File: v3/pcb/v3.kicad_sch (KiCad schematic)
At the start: 421 parts, among them J1 USB_C_Receptacle_USB2.0, J2 Conn_01x21, SW1 SW_Push, SW10 SW_Push, SW11 SW_Push, SW12 SW_Push, SW13 SW_Push, SW14 SW_Push, SW15 SW_Push, SW16 SW_Push, SW17 SW_Push, SW18 SW_Push, SW19 SW_Push, SW2 SW_Push, SW20 SW_Push, SW21 SW_Push, SW22 SW_Push, SW23 SW_Push, SW24 SW_Push, SW25 SW_Push, SW26 SW_Push, SW27 SW_Push, SW28 SW_Push, SW29 SW_Push, SW3 SW_Push, SW30 SW_Push, SW31 SW_Push, SW32 SW_Push, SW33 SW_Push, SW34 SW_Push, SW35 SW_Push, SW36 SW_Push, SW37 SW_Push, SW38 SW_Push, SW39 SW_Push, SW4 SW_Push, SW40 SW_Push, SW41 SW_Push, SW42 SW_Push, SW43 SW_Push, SW44 SW_Push, SW45 SW_Push, SW46 SW_Push, SW47 SW_Push, SW48 SW_Push, SW49 SW_Push, SW5 SW_Push, SW50 SW_Push, SW51 SW_Push, SW52 SW_Push, SW53 SW_Push, SW54 SW_Push, SW55 SW_Push, SW56 SW_Push, SW57 SW_Push, SW58 SW_Push, SW59 SW_Push, SW6 SW_Push, SW60 SW_Push, SW61 SW_Push, SW62 SW_Push, SW63 SW_Push, SW64 SW_Push, SW65 SW_Push, SW66 SW_Push, SW67 SW_Push, SW68 SW_Push, SW69 SW_Push, SW7 SW_Push, SW70 SW_Push, SW71 SW_Push, SW72 SW_Push, SW73 SW_Push, SW74 SW_Push, SW75 SW_Push, SW76 SW_Push, SW77 SW_Push, SW78 SW_Push, SW79 SW_Push, SW8 SW_Push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

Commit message: Add some part numbers and start adding row tracks
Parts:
- C1, C10, C11, C12, C13, C14, C15, C16, C17, C18, C19, C2, C20, C21, C22, C23, C24, C25, C26, C27, C28, C29, C3, C30, C31, C32, C33, C34, C35, C36, C37, C38, C39, C4, C40, C41, C42, C43, C44, C45, C46, C47, C48, C49, C5, C50, C51, C52, C53, C54, C55, C56, C57, C58, C59, C6, C60, C61, C62, C63, C64, C65, C66, C67, C68, C69, C7, C70, C71, C72, C73, C74, C75, C76, C77, C78, C79, C8, C80, C81, C82, C83, C84, C85, C86, C87, C88, C89, C9, C90, C91, C92, C93, C94, C95, C96, C97, C98, C99: LCSC Part C14663 -> C14663
- D1, D10, D11, D12, D13, D14, D15, D16, D17, D18, D19, D2, D20, D21, D22, D23, D24, D25, D26, D27, D28, D29, D3, D30, D31, D32, D33, D34, D35, D36, D37, D38, D39, D4, D40, D41, D42, D43, D44, D45, D46, D47, D48, D49, D5, D50, D51, D52, D53, D54, D55, D56, D57, D58, D59, D6, D60, D61, D62, D63, D64, D65, D66, D67, D68, D69, D7, D70, D71, D72, D73, D74, D75, D76, D77, D78, D79, D8, D80, D81, D82, D83, D84, D85, D86, D87, D88, D89, D9, D90, D91, D92, D93, D94, D95, D96, D97, D98, D99: footprint Diode_SMD:D_SOD-323F -> prettylib:D_SOD-123; symbol Device:D -> Diode:1N4148; LCSC Part (none) -> C81598
- FB1: LCSC C668229 -> (none); LCSC Part (none) -> C668229
- J1: LCSC Part (none) -> C165948
- R1, R2: LCSC C104384 -> (none); LCSC Part (none) -> C104384
- RGB1, RGB10, RGB11, RGB12, RGB13, RGB14, RGB15, RGB16, RGB17, RGB18, RGB19, RGB2, RGB20, RGB21, RGB22, RGB23, RGB24, RGB25, RGB26, RGB27, RGB28, RGB29, RGB3, RGB30, RGB31, RGB32, RGB33, RGB34, RGB35, RGB36, RGB37, RGB38, RGB39, RGB4, RGB40, RGB41, RGB42, RGB43, RGB44, RGB45, RGB46, RGB47, RGB48, RGB49, RGB5, RGB50, RGB51, RGB52, RGB53, RGB54, RGB55, RGB56, RGB57, RGB58, RGB59, RGB6, RGB60, RGB61, RGB62, RGB63, RGB64, RGB65, RGB66, RGB67, RGB68, RGB69, RGB7, RGB70, RGB71, RGB72, RGB73, RGB74, RGB75, RGB76, RGB77, RGB78, RGB79, RGB8, RGB80, RGB81, RGB82, RGB83, RGB84, RGB85, RGB86, RGB87, RGB88, RGB89, RGB9, RGB90, RGB91, RGB92, RGB93, RGB94, RGB95, RGB96, RGB97, RGB98, RGB99: JLCPCB BOM 0 -> 1; LCSC Part (none) -> C5149201
- RGB_LOGO1, RGB_LOGO2, RGB_LOGO3, RGB_LOGO4: LCSC Part (none) -> C5149201
- SW1, SW10, SW11, SW12, SW13, SW14, SW15, SW16, SW17, SW18, SW19, SW2, SW20, SW21, SW22, SW23, SW24, SW25, SW26, SW27, SW28, SW29, SW3, SW30, SW31, SW32, SW33, SW34, SW35, SW36, SW37, SW38, SW39, SW4, SW40, SW41, SW42, SW43, SW44, SW45, SW46, SW47, SW48, SW49, SW5, SW50, SW51, SW52, SW53, SW54, SW55, SW56, SW57, SW58, SW59, SW6, SW60, SW61, SW62, SW63, SW64, SW65, SW66, SW67, SW68, SW69, SW7, SW70, SW71, SW72, SW73, SW74, SW75, SW76, SW77, SW78, SW79, SW8, SW80, SW81, SW82, SW83, SW84, SW85, SW86, SW87, SW88, SW89, SW9, SW90, SW91, SW92, SW93, SW94, SW95, SW96, SW97, SW98, SW99: LCSC Part (none) -> C5184526
- U2: LCSC Part (none) -> C139353

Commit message: PCB might be ready for manufacturing
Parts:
- SW1, SW10, SW11, SW12, SW13, SW14, SW15, SW16, SW17, SW18, SW19, SW2, SW20, SW21, SW22, SW23, SW24, SW25, SW26, SW28, SW29, SW3, SW30, SW31, SW32, SW33, SW34, SW35, SW36, SW37, SW38, SW39, SW4, SW40, SW41, SW42, SW43, SW44, SW45, SW46, SW47, SW48, SW49, SW5, SW50, SW52, SW53, SW54, SW55, SW56, SW57, SW58, SW59, SW6, SW60, SW61, SW62, SW63, SW65, SW66, SW67, SW68, SW69, SW7, SW70, SW71, SW72, SW73, SW74, SW75, SW76, SW77, SW78, SW79, SW8, SW80, SW81, SW82, SW83, SW84, SW85, SW87, SW88, SW89, SW9, SW90, SW93, SW94, SW95, SW96, SW97, SW99: footprint prettylib:MX_KAILH_SOCKET_1U -> zekeyboard:MX_KAILH_SOCKET_1U_NONFLIP
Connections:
- no-connect marks 38 -> 36

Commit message: Ready for production
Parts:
- C1, C10, C11, C12, C13, C14, C15, C16, C17, C18, C19, C2, C20, C21, C22, C23, C24, C25, C26, C27, C28, C29, C3, C30, C31, C32, C33, C34, C35, C36, C37, C38, C39, C4, C40, C41, C42, C43, C44, C45, C46, C47, C48, C49, C5, C50, C51, C52, C53, C54, C55, C56, C57, C58, C59, C6, C60, C61, C62, C63, C64, C65, C66, C67, C68, C69, C7, C70, C71, C72, C73, C74, C75, C76, C77, C78, C79, C8, C80, C81, C82, C83, C84, C85, C86, C87, C88, C89, C9, C90, C91, C92, C93, C94, C95, C96, C97, C98, C99: footprint prettylib:SMD-0603 -> Capacitor_SMD:C_0603_1608Metric; LCSC (none) -> C14663
- D1, D10, D11, D12, D13, D14, D15, D16, D17, D18, D19, D2, D20, D21, D22, D23, D24, D25, D26, D27, D28, D29, D3, D30, D31, D32, D33, D34, D35, D36, D37, D38, D39, D4, D40, D41, D42, D43, D44, D45, D46, D47, D48, D49, D5, D50, D51, D52, D53, D54, D55, D56, D57, D58, D59, D6, D60, D61, D62, D63, D64, D65, D66, D67, D68, D69, D7, D70, D71, D72, D73, D74, D75, D76, D77, D78, D79, D8, D80, D81, D82, D83, D84, D85, D86, D87, D88, D89, D9, D90, D91, D92, D93, D94, D95, D96, D97, D98, D99: footprint prettylib:D_SOD-123 -> Diode_SMD:D_SOD-123; LCSC (none) -> C81598
- FB1: LCSC (none) -> C668229
- J1: LCSC (none) -> C165948
- R1, R2: LCSC (none) -> C104384
- RGB1, RGB10, RGB11, RGB12, RGB13, RGB14, RGB15, RGB16, RGB17, RGB18, RGB19, RGB2, RGB20, RGB21, RGB22, RGB23, RGB24, RGB25, RGB26, RGB27, RGB28, RGB29, RGB3, RGB30, RGB31, RGB32, RGB33, RGB34, RGB35, RGB36, RGB37, RGB38, RGB39, RGB4, RGB40, RGB41, RGB42, RGB43, RGB44, RGB45, RGB46, RGB47, RGB48, RGB49, RGB5, RGB50, RGB51, RGB52, RGB53, RGB54, RGB55, RGB56, RGB57, RGB58, RGB59, RGB6, RGB60, RGB61, RGB62, RGB63, RGB64, RGB65, RGB66, RGB67, RGB68, RGB69, RGB7, RGB70, RGB71, RGB72, RGB73, RGB74, RGB75, RGB76, RGB77, RGB78, RGB79, RGB8, RGB80, RGB81, RGB82, RGB83, RGB84, RGB85, RGB86, RGB87, RGB88, RGB89, RGB9, RGB90, RGB91, RGB92, RGB93, RGB94, RGB95, RGB96, RGB97, RGB98, RGB99, RGB_LOGO1, RGB_LOGO2, RGB_LOGO3, RGB_LOGO4: footprint prettylib:SK6812_mini_e_flipable -> zekeyboard:SK6812_mini_e_flipable; LCSC (none) -> C5149201
- SW1, SW10, SW11, SW12, SW13, SW14, SW15, SW16, SW17, SW18, SW19, SW2, SW20, SW21, SW22, SW23, SW24, SW25, SW26, SW28, SW29, SW3, SW30, SW31, SW32, SW33, SW34, SW35, SW36, SW37, SW38, SW39, SW4, SW40, SW41, SW42, SW43, SW44, SW45, SW46, SW47, SW48, SW49, SW5, SW50, SW52, SW53, SW54, SW55, SW56, SW57, SW58, SW59, SW6, SW60, SW61, SW62, SW63, SW65, SW66, SW67, SW68, SW69, SW7, SW70, SW71, SW72, SW73, SW74, SW75, SW76, SW77, SW78, SW79, SW8, SW80, SW81, SW82, SW83, SW84, SW85, SW87, SW88, SW89, SW9, SW90, SW93, SW94, SW95, SW96, SW97, SW99: footprint zekeyboard:MX_KAILH_SOCKET_1U_NONFLIP -> marbastlib-mx:SW_MX_HS_1u; LCSC (none) -> C5184526
- SW27, SW64, SW91, SW92, SW98: footprint zekeyboard:MX_KAILH_SOCKET_2U_STAB -> marbastlib-mx:SW_MX_HS_1u; LCSC (none) -> C5184526
- SW51, SW86: footprint zekeyboard:MX_KAILH_SOCKET_2U_STAB_VERT -> marbastlib-mx:SW_MX_HS_1u; LCSC (none) -> C5184526
- U2: LCSC (none) -> C139353
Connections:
- no-connect marks 36 -> 33

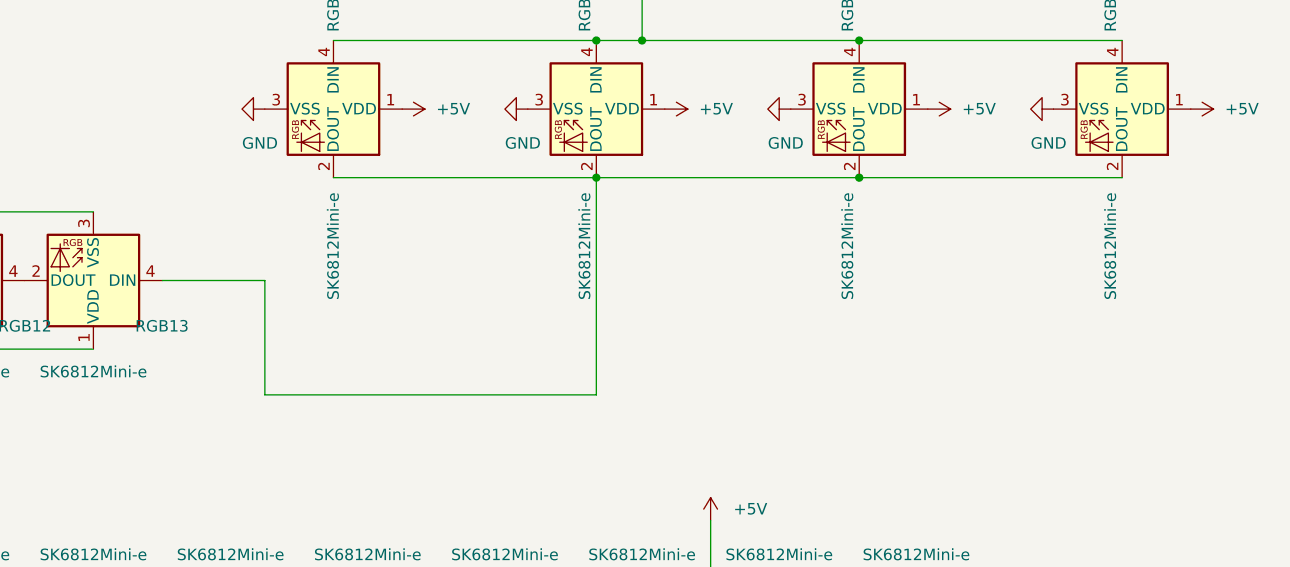
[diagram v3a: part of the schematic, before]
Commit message: Fix the mistakes of the produced PCB
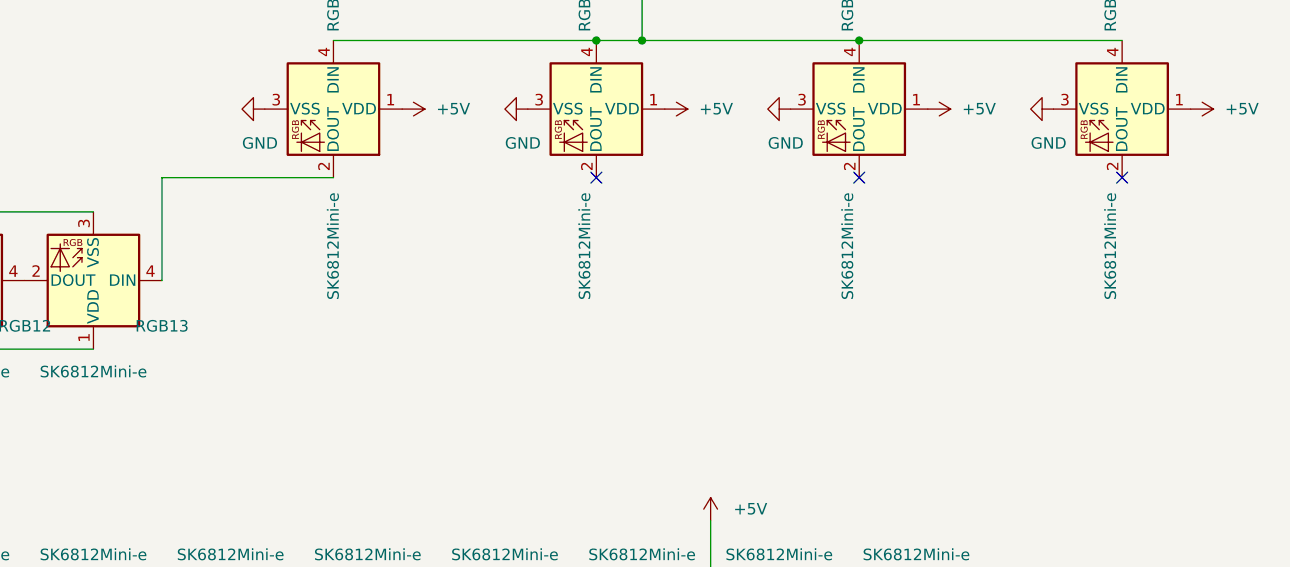
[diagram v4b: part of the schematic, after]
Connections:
- new net: RGB13.4 (DIN), RGB_LOGO1.2 (DOUT)
- now unconnected: RGB_LOGO2.2 (DOUT), RGB_LOGO3.2 (DOUT), RGB_LOGO4.2 (DOUT)
- no-connect marks 33 -> 36
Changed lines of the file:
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@@
   (junction (at 246.38 138.43) (diameter 0) (color 0 0 0 0)
   )
-  (junction (at 304.8 217.17) (diameter 0) (color 0 0 0 0)
-  )
   (junction (at 203.2 312.42) (diameter 0) (color 0 0 0 0)
   )
@@
   (junction (at 575.31 299.72) (diameter 0) (color 0 0 0 0)
   )
-  (junction (at 334.01 217.17) (diameter 0) (color 0 0 0 0)
-  )
   (junction (at 420.37 261.62) (diameter 0) (color 0 0 0 0)
   )
@@
   (no_connect (at 575.31 88.9))
   (no_connect (at 575.31 78.74))
+  (no_connect (at 334.01 217.17))
   (no_connect (at 575.31 99.06))
+  (no_connect (at 304.8 217.17))
   (no_connect (at 575.31 111.76))
   (no_connect (at 575.31 139.7))
@@
   (no_connect (at 516.89 149.86))
   (no_connect (at 575.31 142.24))
+  (no_connect (at 363.22 217.17))
   (no_connect (at 575.31 104.14))
   (no_connect (at 684.53 63.5))
@@
     (stroke (width 0) (type default) (color 0 0 0 0))
   )
-  (wire (pts (xy 275.59 217.17) (xy 304.8 217.17))
-    (stroke (width 0) (type default) (color 0 0 0 0))
-  )
   (wire (pts (xy 209.55 107.95) (xy 210.82 107.95))
     (stroke (width 0) (type default) (color 0 0 0 0))
@@
     (stroke (width 0) (type default) (color 0 0 0 0))
   )
-  (wire (pts (xy 267.97 241.3) (xy 267.97 228.6))
-    (stroke (width 0) (type default) (color 0 0 0 0))
-  )
   (wire (pts (xy 162.56 53.34) (xy 162.56 67.31))
     (stroke (width 0) (type default) (color 0 0 0 0))
@@
     (stroke (width 0) (type default) (color 0 0 0 0))
   )
-  (wire (pts (xy 304.8 241.3) (xy 267.97 241.3))
-    (stroke (width 0) (type default) (color 0 0 0 0))
-  )
   (wire (pts (xy 52.07 76.2) (xy 52.07 77.47))
     (stroke (width 0) (type default) (color 0 0 0 0))
@@
     (stroke (width 0) (type default) (color 0 0 0 0))
   )
-  (wire (pts (xy 267.97 228.6) (xy 256.54 228.6))
-    (stroke (width 0) (type default) (color 0 0 0 0))
-  )
   (wire (pts (xy 175.26 67.31) (xy 175.26 68.58))
     (stroke (width 0) (type default) (color 0 0 0 0))
@@
     (stroke (width 0) (type default) (color 0 0 0 0))
   )
+  (wire (pts (xy 256.54 217.17) (xy 275.59 217.17))
+    (stroke (width 0) (type default) (color 0 0 0 0))
+  )
   (wire (pts (xy 109.22 53.34) (xy 109.22 67.31))
     (stroke (width 0) (type default) (color 0 0 0 0))
@@
     (stroke (width 0) (type default) (color 0 0 0 0))
   )
-  (wire (pts (xy 304.8 217.17) (xy 304.8 241.3))
-    (stroke (width 0) (type default) (color 0 0 0 0))
-  )
   (wire (pts (xy 40.64 148.59) (xy 39.37 148.59))
     (stroke (width 0) (type default) (color 0 0 0 0))
@@
     (stroke (width 0) (type default) (color 0 0 0 0))
   )
-  (wire (pts (xy 304.8 217.17) (xy 334.01 217.17))
-    (stroke (width 0) (type default) (color 0 0 0 0))
-  )
   (wire (pts (xy 636.27 355.6) (xy 646.43 355.6))
     (stroke (width 0) (type default) (color 0 0 0 0))
@@
     (stroke (width 0) (type default) (color 0 0 0 0))
   )
-  (wire (pts (xy 334.01 217.17) (xy 363.22 217.17))
-    (stroke (width 0) (type default) (color 0 0 0 0))
-  )
   (wire (pts (xy 353.06 118.11) (xy 370.84 118.11))
     (stroke (width 0) (type default) (color 0 0 0 0))
@@
     (stroke (width 0) (type default) (color 0 0 0 0))
   )
+  (wire (pts (xy 256.54 217.17) (xy 256.54 228.6))
+    (stroke (width 0) (type default) (color 0 0 0 0))
+  )

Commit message: Update PCB for layout-4
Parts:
- added C100: 100n, Capacitor_SMD:C_0603_1608Metric, symbol YAEMK:C
- added D100: D, Diode_SMD:D_SOD-123, symbol Diode:1N4148
- added RGB100: SK6812Mini-e, zekeyboard:SK6812_mini_e_flipable, symbol YAEMK:SK6812MINI-E
- added SW100: SW_Push, marbastlib-mx:SW_MX_HS_1u, symbol Switch:SW_Push
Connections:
- net +5V: now also C100.1, RGB100.1 (VDD)
- net COL1: now also SW100.1
- net GND: now also C100.2, RGB100.3 (VSS)
- net ROW4: now also D100.1 (K)
- net at RGB70.2 (DOUT): now also RGB100.4 (DIN); no longer RGB69.4 (DIN)
- new net: D100.2 (A), SW100.2
- new net: RGB100.2 (DOUT), RGB69.4 (DIN)
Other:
- moved on the sheet: C61, C62, C63, C64, C65, C66, C67, C68, C69, RGB70, RGB71, RGB72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

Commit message: Ready for production 2
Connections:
- net USB_D+: no longer U1.60 (A25_D+)
- net USB_D-: no longer U1.59 (A26_D-)
- no-connect marks 36 -> 38
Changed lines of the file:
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@@
   (no_connect (at 575.31 139.7))
   (no_connect (at 575.31 68.58))
+  (no_connect (at 575.31 127))
   (no_connect (at 684.53 66.04))
   (no_connect (at 575.31 60.96))
@@
   (no_connect (at 516.89 157.48))
   (no_connect (at 575.31 149.86))
+  (no_connect (at 575.31 129.54))
   (no_connect (at 575.31 93.98))
   (wire (pts (xy 325.12 297.18) (xy 340.36 297.18))
@@
     )
   )
-  (global_label "USB_D+" (shape input) (at 575.31 127 0) (fields_autoplaced)
-    (effects (font (size 1.27 1.27)) (justify left))
-    (property "Intersheet References" "${INTERSHEET_REFS}" (id 0) (at 585.3431 126.9206 0)
-      (effects (font (size 1.27 1.27)) (justify left) hide)
-    )
-  )
   (global_label "COL16" (shape input) (at 322.58 53.34 90) (fields_autoplaced)
     (effects (font (size 1.27 1.27)) (justify left))
@@
     )
   )
-  (global_label "USB_D-" (shape input) (at 575.31 129.54 0) (fields_autoplaced)
-    (effects (font (size 1.27 1.27)) (justify left))
-    (property "Intersheet References" "${INTERSHEET_REFS}" (id 0) (at 585.3431 129.4606 0)
-      (effects (font (size 1.27 1.27)) (justify left) hide)
-    )
-  )
